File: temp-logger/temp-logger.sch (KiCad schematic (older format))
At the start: 22 parts, among them J1 USB_OTG, J2 CONN_01X03, SW1 SW_Push, SW2 SW_Push, U1 AP1117-33, U2 ESP-12E, U3 HTU21D

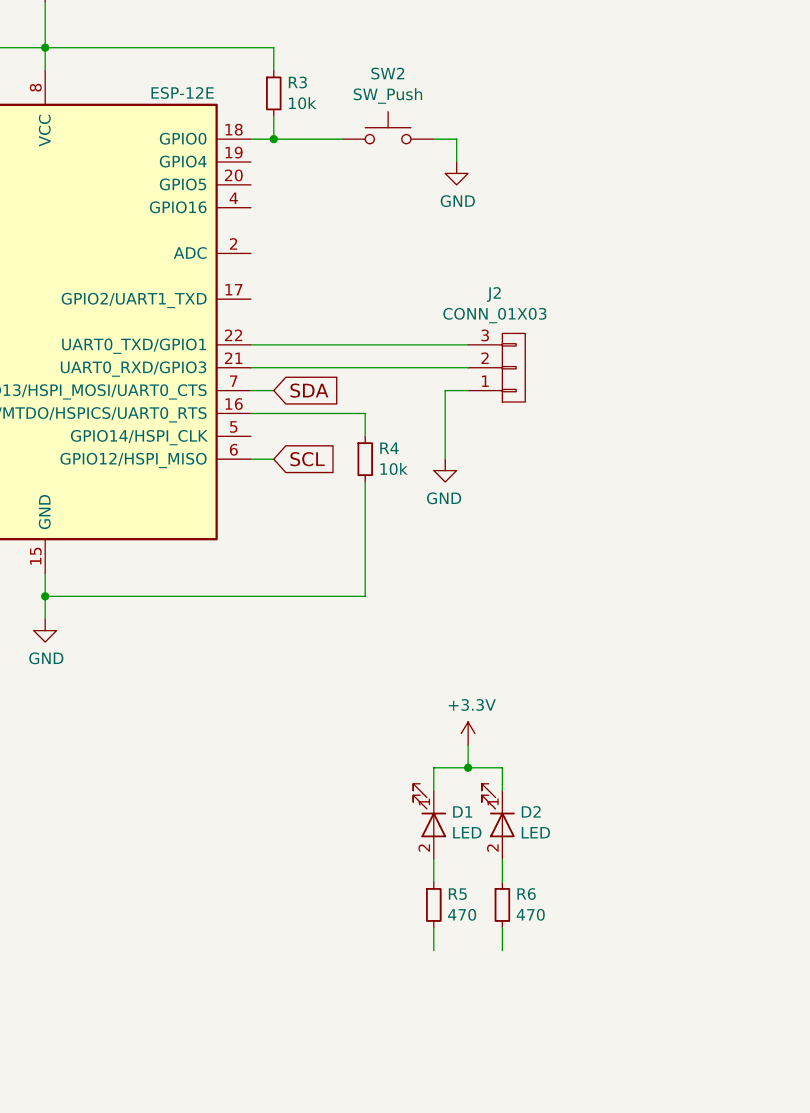
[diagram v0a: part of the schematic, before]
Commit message: Hooked up LEDs
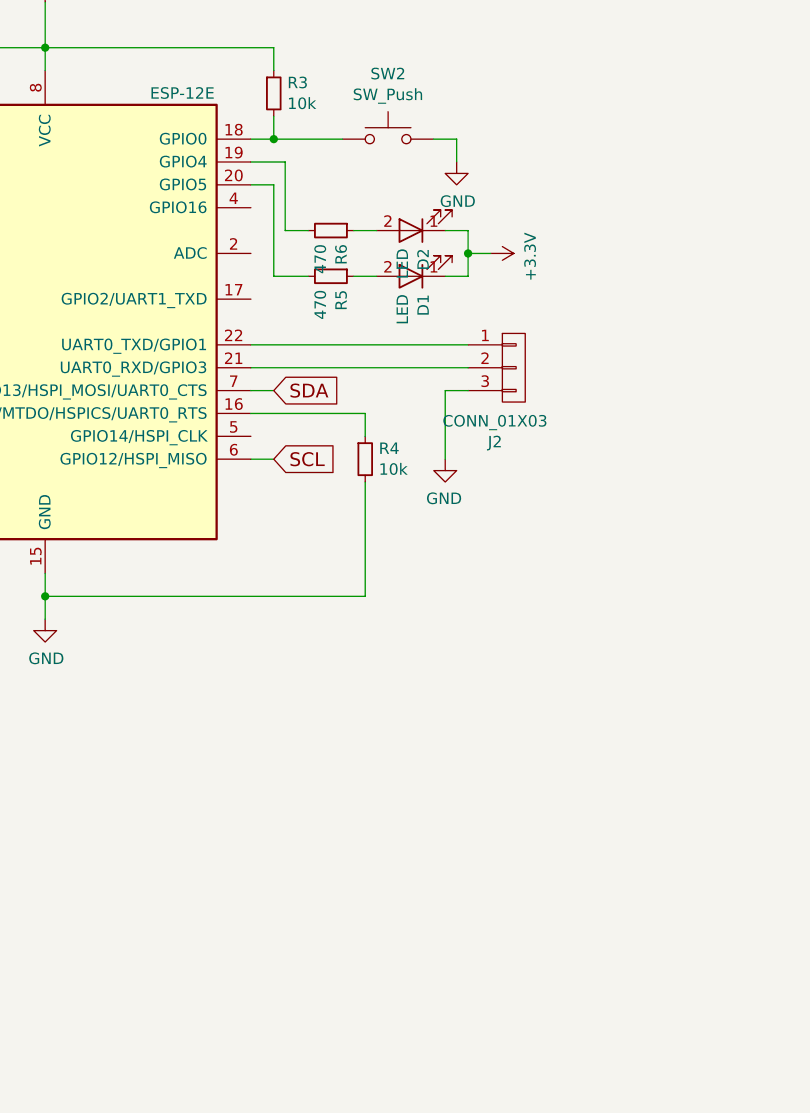
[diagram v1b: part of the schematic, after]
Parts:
- renumbered D2 to D1, D1 to D2, R6 to R5, R5 to R6
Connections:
- net GND: now also J2.3 (P3); no longer J2.1 (P1)
- net at U2.19 (GPIO4): now also R6.2
- net at U2.20 (GPIO5): now also R5.2
- net at U2.22 (UART0_TXD/GPIO1): now also J2.1 (P1); no longer J2.3 (P3)
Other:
- moved on the sheet: D1, D2, R5, R6
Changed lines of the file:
@@
+$EndComp
+$Comp
+L LED D2
+U 1 1 5A08A8EC
+P 4100 2450
+F 0 "D2" V 4045 2528 50  0000 L CNN
+F 1 "LED" V 4136 2528 50  0000 L CNN
+F 2 "LEDs:LED_0603" H 4100 2450 50  0001 C CNN
+F 3 "~" H 4100 2450 50  0001 C CNN
+	1    4100 2450
+	-1   0    0    1
 $EndComp
 $Comp
 L LED D1
-U 1 1 5A08A8EC
-P 4200 5050
-F 0 "D1" V 4145 5128 50  0000 L CNN
-F 1 "LED" V 4236 5128 50  0000 L CNN
-F 2 "LEDs:LED_0603" H 4200 5050 50  0001 C CNN
-F 3 "~" H 4200 5050 50  0001 C CNN
-	1    4200 5050
+U 1 1 5A08A96D
+P 4100 2650
+F 0 "D1" V 4045 2728 50  0000 L CNN
+F 1 "LED" V 4136 2728 50  0000 L CNN
+F 2 "LEDs:LED_0603" H 4100 2650 50  0001 C CNN
+F 3 "~" H 4100 2650 50  0001 C CNN
+	1    4100 2650
+	-1   0    0    1
+$EndComp
+$Comp
+L R_Small R6
+U 1 1 5A08AA11
+P 3750 2450
+F 0 "R6" H 3809 2496 50  0000 L CNN
+F 1 "470" H 3809 2405 50  0000 L CNN
+F 2 "Resistors_SMD:R_0603" H 3750 2450 50  0001 C CNN
+F 3 "" H 3750 2450 50  0001 C CNN
+	1    3750 2450
 	0    1    1    0
 $EndComp
 $Comp
-L LED D2
-U 1 1 5A08A96D
-P 4500 5050
-F 0 "D2" V 4445 5128 50  0000 L CNN
-F 1 "LED" V 4536 5128 50  0000 L CNN
-F 2 "LEDs:LED_0603" H 4500 5050 50  0001 C CNN
-F 3 "~" H 4500 5050 50  0001 C CNN
-	1    4500 5050
+L R_Small R5
+U 1 1 5A08AAAC
+P 3750 2650
+F 0 "R5" H 3809 2696 50  0000 L CNN
+F 1 "470" H 3809 2605 50  0000 L CNN
+F 2 "Resistors_SMD:R_0603" H 3750 2650 50  0001 C CNN
+F 3 "" H 3750 2650 50  0001 C CNN
+	1    3750 2650
 	0    1    1    0
-$EndComp
-$Comp
-L R_Small R5
-U 1 1 5A08AA11
-P 4200 5400
-F 0 "R5" H 4259 5446 50  0000 L CNN
-F 1 "470" H 4259 5355 50  0000 L CNN
-F 2 "Resistors_SMD:R_0603" H 4200 5400 50  0001 C CNN
-F 3 "" H 4200 5400 50  0001 C CNN
-	1    4200 5400
-	1    0    0    -1
-$EndComp
-$Comp
-L R_Small R6
-U 1 1 5A08AAAC
-P 4500 5400
-F 0 "R6" H 4559 5446 50  0000 L CNN
-F 1 "470" H 4559 5355 50  0000 L CNN
-F 2 "Resistors_SMD:R_0603" H 4500 5400 50  0001 C CNN
-F 3 "" H 4500 5400 50  0001 C CNN
-	1    4500 5400
-	1    0    0    -1
 $EndComp
 $Comp
 L +3.3V #PWR09
 U 1 1 5A08AB9F
-P 4350 4700
-F 0 "#PWR09" H 4350 4550 50  0001 C CNN
-F 1 "+3.3V" H 4365 4873 50  0000 C CNN
-F 2 "" H 4350 4700 50  0001 C CNN
-F 3 "" H 4350 4700 50  0001 C CNN
-	1    4350 4700
-	1    0    0    -1
+P 4450 2550
+F 0 "#PWR09" H 4450 2400 50  0001 C CNN
+F 1 "+3.3V" H 4465 2723 50  0000 C CNN
+F 2 "" H 4450 2550 50  0001 C CNN
+F 3 "" H 4450 2550 50  0001 C CNN
+	1    4450 2550
+	0    1    1    0
 $EndComp
 NoConn ~ 1600 2450
@@
 F 3 "" H 4550 3050 50  0001 C CNN
 	1    4550 3050
-	1    0    0    1
+	1    0    0    -1
 $EndComp
 Wire Wire Line
@@
 Connection ~ 2500 4050
 Wire Wire Line
-	4200 5200 4200 5300
-Wire Wire Line
-	4500 5200 4500 5300
-Wire Wire Line
-	4200 4900 4200 4800
-Wire Wire Line
-	4200 4800 4500 4800
-Wire Wire Line
-	4500 4800 4500 4900
-Wire Wire Line
-	4350 4700 4350 4800
-Connection ~ 4350 4800
-Wire Wire Line
-	4200 5500 4200 5600
-Wire Wire Line
-	4500 5500 4500 5600
+	3950 2450 3850 2450
+Wire Wire Line
+	3950 2650 3850 2650
+Wire Wire Line
+	4250 2450 4350 2450
+Wire Wire Line
+	4350 2650 4250 2650
+Wire Wire Line
+	4450 2550 4350 2550
+Connection ~ 4350 2550
+Wire Wire Line
+	3650 2450 3550 2450
+Wire Wire Line
+	3500 2650 3650 2650
 Connection ~ 1500 2050
 Wire Wire Line
@@
 Wire Wire Line
 	3500 3450 3400 3450
+Wire Wire Line
+	4350 2450 4350 2650
+Wire Wire Line
+	3400 2150 3550 2150
+Wire Wire Line
+	3550 2150 3550 2450
+Wire Wire Line
+	3400 2250 3500 2250
+Wire Wire Line
+	3500 2250 3500 2650
 $EndSCHEMATC

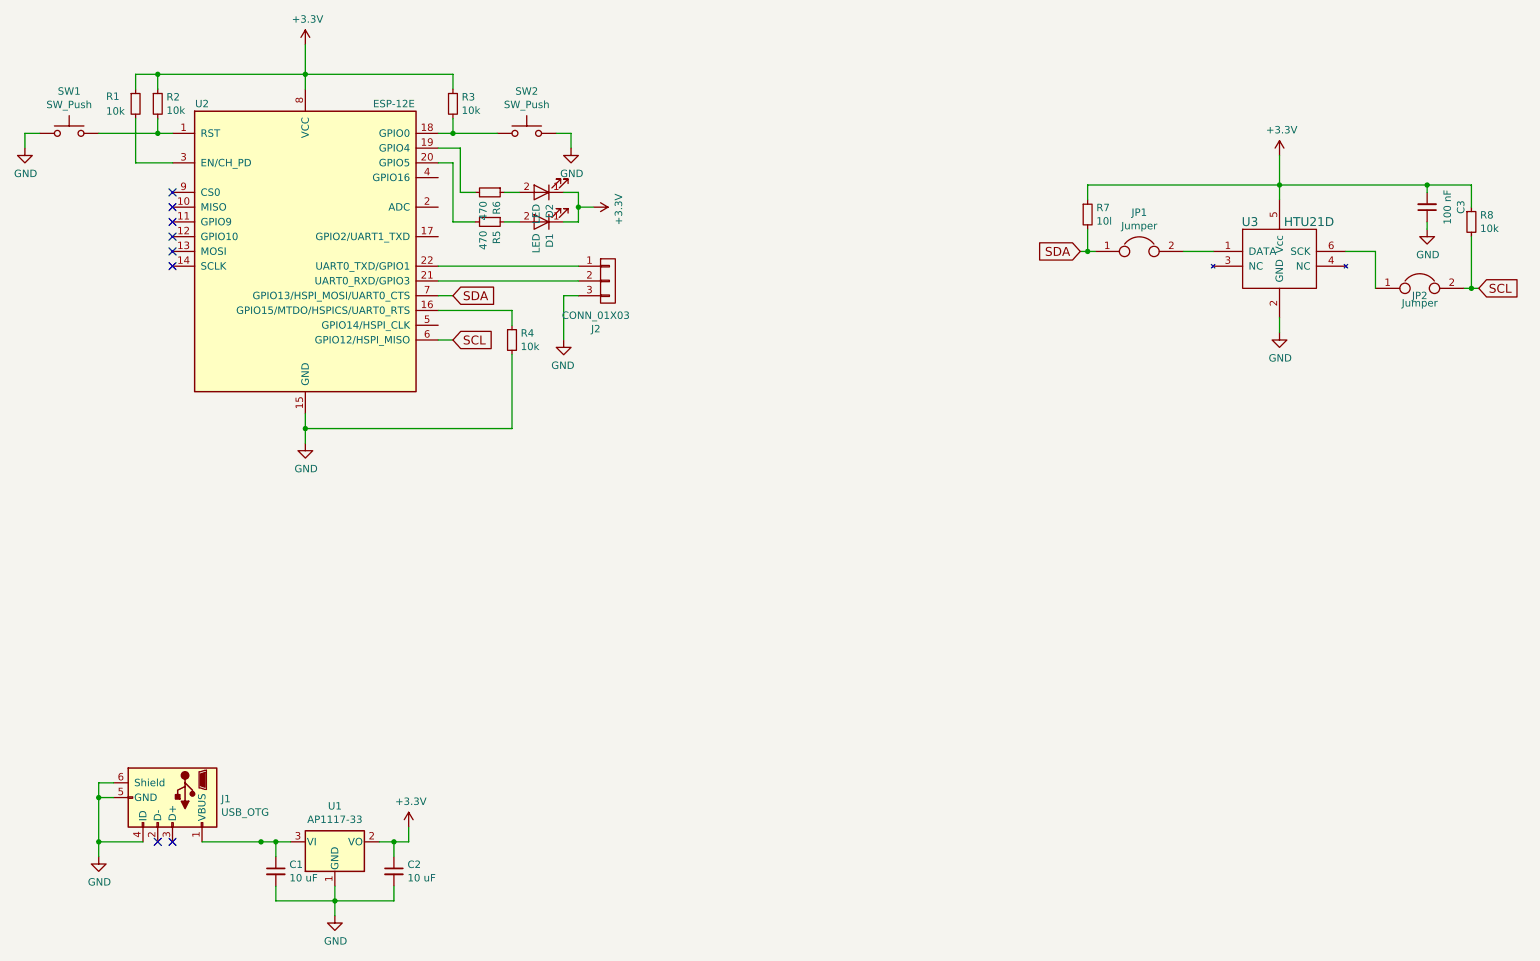
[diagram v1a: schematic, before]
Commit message: Redid layout to make soldering and programming easier
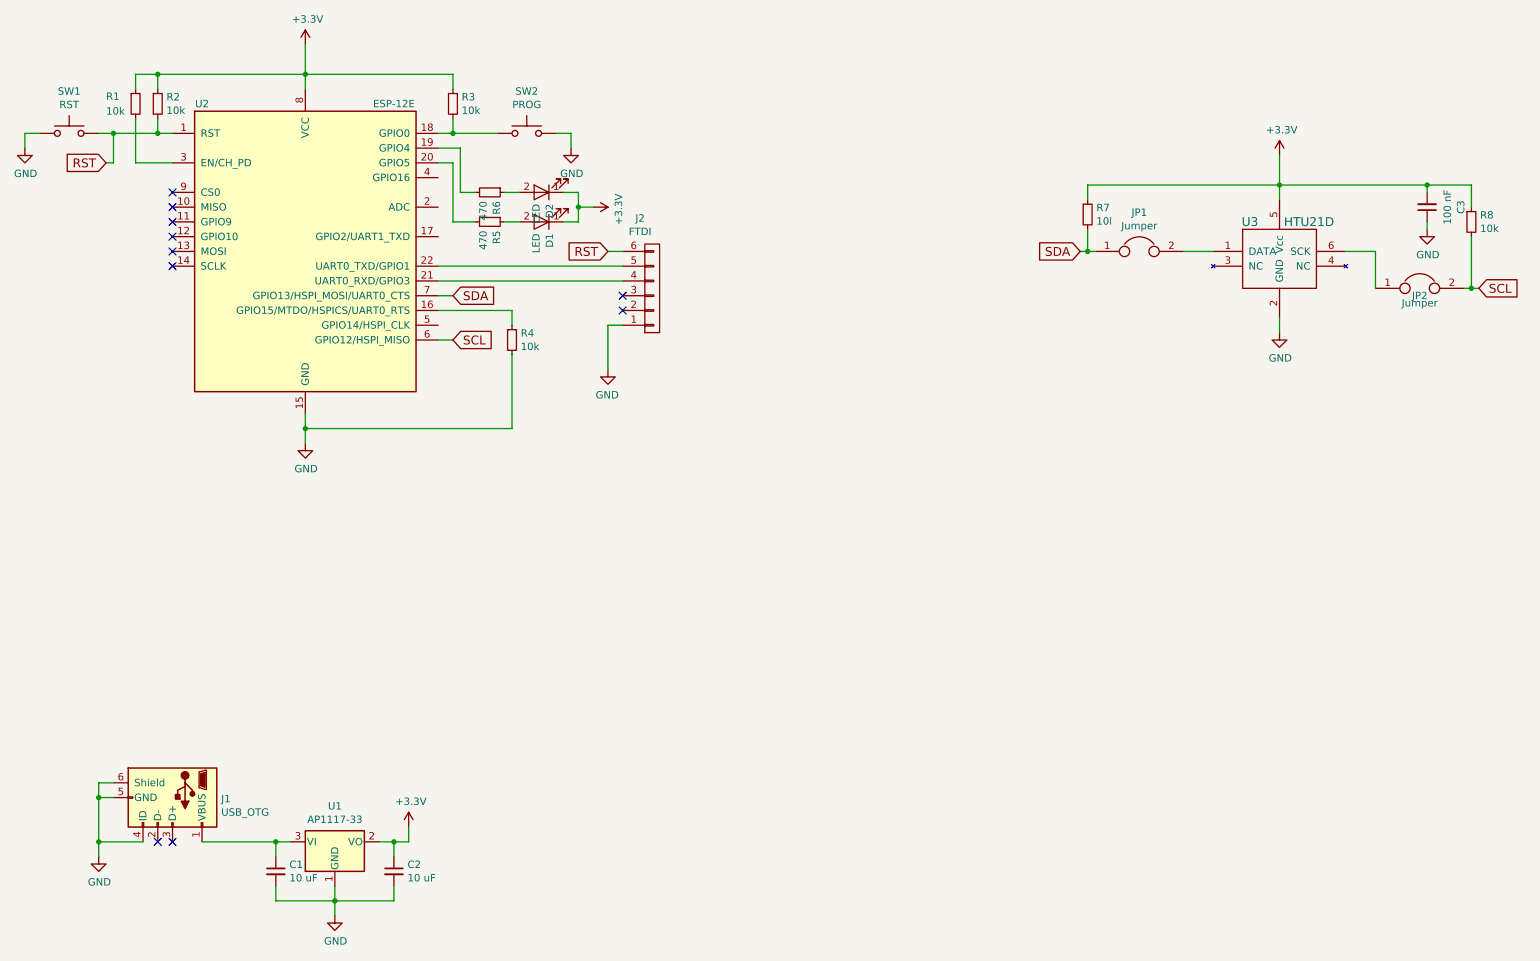
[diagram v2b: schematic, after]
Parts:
- removed J2: CONN_01X03, Pin_Headers:Pin_Header_Straight_1x03_Pitch1.00mm_SMD_Pin1Right, symbol CONN_01X03
- added J2: FTDI, Pin_Headers:Pin_Header_Straight_1x06_Pitch2.54mm, symbol CONN_01X06
- C1, C2: footprint Capacitors_SMD:C_1206 -> Capacitors_SMD:C_1206_HandSoldering
- C3: footprint Capacitors_SMD:C_0603 -> Capacitors_SMD:C_0603_HandSoldering
- D1, D2: footprint LEDs:LED_0603 -> LEDs:LED_1206_HandSoldering
- JP1, JP2, R1, R2, R3, R4, R5, R6, R7, R8: footprint Resistors_SMD:R_0603 -> Resistors_SMD:R_0603_HandSoldering
- SW1: value SW_Push -> RST
- SW2: value SW_Push -> PROG
- U1: footprint TO_SOT_Packages_SMD:SOT-223-3Lead_TabPin2 -> TO_SOT_Packages_SMD:SOT-223
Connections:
- net GND: now also J2.1 (P1)
- net RST: now reaches R2.2, SW1.2, U2.1 (RST)
- net RST: now also J2.6 (P6)
- net at U2.21 (UART0_RXD/GPIO3): now also J2.4 (P4)
- net at U2.22 (UART0_TXD/GPIO1): now also J2.5 (P5)
- no-connect marks 8 -> 10
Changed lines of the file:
@@
 F 0 "U1" H 2700 7092 50  0000 C CNN
 F 1 "AP1117-33" H 2700 7001 50  0000 C CNN
-F 2 "TO_SOT_Packages_SMD:SOT-223-3Lead_TabPin2" H 2700 7050 50  0001 C CNN
+F 2 "TO_SOT_Packages_SMD:SOT-223" H 2700 7050 50  0001 C CNN
 F 3 "http://www.diodes.com/datasheets/AP1117.pdf" H 2800 6600 50  0001 C CNN
 	1    2700 6850
@@
 F 0 "C3" V 9871 2550 50  0000 C CNN
 F 1 "100 nF" V 9962 2550 50  0000 C CNN
-F 2 "Capacitors_SMD:C_0603" H 10100 2550 50  0001 C CNN
+F 2 "Capacitors_SMD:C_0603_HandSoldering" H 10100 2550 50  0001 C CNN
 F 3 "" H 10100 2550 50  0001 C CNN
 	1    10100 2550
@@
 F 0 "C1" H 2392 7096 50  0000 L CNN
 F 1 "10 uF" H 2392 7005 50  0000 L CNN
-F 2 "Capacitors_SMD:C_1206" H 2300 7050 50  0001 C CNN
+F 2 "Capacitors_SMD:C_1206_HandSoldering" H 2300 7050 50  0001 C CNN
 F 3 "" H 2300 7050 50  0001 C CNN
 	1    2300 7050
@@
 F 0 "C2" H 3192 7096 50  0000 L CNN
 F 1 "10 uF" H 3192 7005 50  0000 L CNN
-F 2 "Capacitors_SMD:C_1206" H 3100 7050 50  0001 C CNN
+F 2 "Capacitors_SMD:C_1206_HandSoldering" H 3100 7050 50  0001 C CNN
 F 3 "" H 3100 7050 50  0001 C CNN
 	1    3100 7050
@@
 F 0 "R2" H 1559 1896 50  0000 L CNN
 F 1 "10k" H 1559 1805 50  0000 L CNN
-F 2 "Resistors_SMD:R_0603" H 1500 1850 50  0001 C CNN
+F 2 "Resistors_SMD:R_0603_HandSoldering" H 1500 1850 50  0001 C CNN
 F 3 "" H 1500 1850 50  0001 C CNN
 	1    1500 1850
@@
 F 0 "R1" H 1150 1900 50  0000 L CNN
 F 1 "10k" H 1150 1800 50  0000 L CNN
-F 2 "Resistors_SMD:R_0603" H 1350 1850 50  0001 C CNN
+F 2 "Resistors_SMD:R_0603_HandSoldering" H 1350 1850 50  0001 C CNN
 F 3 "" H 1350 1850 50  0001 C CNN
 	1    1350 1850
@@
 F 0 "R3" H 3559 1896 50  0000 L CNN
 F 1 "10k" H 3559 1805 50  0000 L CNN
-F 2 "Resistors_SMD:R_0603" H 3500 1850 50  0001 C CNN
+F 2 "Resistors_SMD:R_0603_HandSoldering" H 3500 1850 50  0001 C CNN
 F 3 "" H 3500 1850 50  0001 C CNN
 	1    3500 1850
@@
 F 0 "R4" H 3959 3496 50  0000 L CNN
 F 1 "10k" H 3959 3405 50  0000 L CNN
-F 2 "Resistors_SMD:R_0603" H 3900 3450 50  0001 C CNN
+F 2 "Resistors_SMD:R_0603_HandSoldering" H 3900 3450 50  0001 C CNN
 F 3 "" H 3900 3450 50  0001 C CNN
 	1    3900 3450
@@
 F 0 "D2" V 4045 2528 50  0000 L CNN
 F 1 "LED" V 4136 2528 50  0000 L CNN
-F 2 "LEDs:LED_0603" H 4100 2450 50  0001 C CNN
+F 2 "LEDs:LED_1206_HandSoldering" H 4100 2450 50  0001 C CNN
 F 3 "~" H 4100 2450 50  0001 C CNN
 	1    4100 2450
@@
 F 0 "D1" V 4045 2728 50  0000 L CNN
 F 1 "LED" V 4136 2728 50  0000 L CNN
-F 2 "LEDs:LED_0603" H 4100 2650 50  0001 C CNN
+F 2 "LEDs:LED_1206_HandSoldering" H 4100 2650 50  0001 C CNN
 F 3 "~" H 4100 2650 50  0001 C CNN
 	1    4100 2650
@@
 F 0 "R6" H 3809 2496 50  0000 L CNN
 F 1 "470" H 3809 2405 50  0000 L CNN
-F 2 "Resistors_SMD:R_0603" H 3750 2450 50  0001 C CNN
+F 2 "Resistors_SMD:R_0603_HandSoldering" H 3750 2450 50  0001 C CNN
 F 3 "" H 3750 2450 50  0001 C CNN
 	1    3750 2450
@@
 F 0 "R5" H 3809 2696 50  0000 L CNN
 F 1 "470" H 3809 2605 50  0000 L CNN
-F 2 "Resistors_SMD:R_0603" H 3750 2650 50  0001 C CNN
+F 2 "Resistors_SMD:R_0603_HandSoldering" H 3750 2650 50  0001 C CNN
 F 3 "" H 3750 2650 50  0001 C CNN
 	1    3750 2650
@@
 F 0 "R7" H 7859 2646 50  0000 L CNN
 F 1 "10l" H 7859 2555 50  0000 L CNN
-F 2 "Resistors_SMD:R_0603" H 7800 2600 50  0001 C CNN
+F 2 "Resistors_SMD:R_0603_HandSoldering" H 7800 2600 50  0001 C CNN
 F 3 "" H 7800 2600 50  0001 C CNN
 	1    7800 2600
@@
 F 0 "R8" H 10459 2696 50  0000 L CNN
 F 1 "10k" H 10459 2605 50  0000 L CNN
-F 2 "Resistors_SMD:R_0603" H 10400 2650 50  0001 C CNN
+F 2 "Resistors_SMD:R_0603_HandSoldering" H 10400 2650 50  0001 C CNN
 F 3 "" H 10400 2650 50  0001 C CNN
 	1    10400 2650
@@
 L GND #PWR012
 U 1 1 5A08CD0F
-P 4250 3450
-F 0 "#PWR012" H 4250 3200 50  0001 C CNN
-F 1 "GND" H 4255 3277 50  0000 C CNN
-F 2 "" H 4250 3450 50  0001 C CNN
-F 3 "" H 4250 3450 50  0001 C CNN
-	1    4250 3450
+P 4550 3650
+F 0 "#PWR012" H 4550 3400 50  0001 C CNN
+F 1 "GND" H 4555 3477 50  0000 C CNN
+F 2 "" H 4550 3650 50  0001 C CNN
+F 3 "" H 4550 3650 50  0001 C CNN
+	1    4550 3650
 	-1   0    0    -1
 $EndComp
@@
 P 900 2050
 F 0 "SW1" H 900 2335 50  0000 C CNN
-F 1 "SW_Push" H 900 2244 50  0000 C CNN
+F 1 "RST" H 900 2244 50  0000 C CNN
 F 2 "Buttons_Switches_SMD:SW_SPST_B3U-1000P" H 900 2250 50  0001 C CNN
 F 3 "" H 900 2250 50  0001 C CNN
@@
 P 4000 2050
 F 0 "SW2" H 4000 2335 50  0000 C CNN
-F 1 "SW_Push" H 4000 2244 50  0000 C CNN
+F 1 "PROG" H 4000 2244 50  0000 C CNN
 F 2 "Buttons_Switches_SMD:SW_SPST_B3U-1000P" H 4000 2250 50  0001 C CNN
 F 3 "" H 4000 2250 50  0001 C CNN
@@
 F 0 "JP1" H 8150 3114 50  0000 C CNN
 F 1 "Jumper" H 8150 3023 50  0000 C CNN
-F 2 "Resistors_SMD:R_0603" H 8150 2850 50  0001 C CNN
+F 2 "Resistors_SMD:R_0603_HandSoldering" H 8150 2850 50  0001 C CNN
 F 3 "" H 8150 2850 50  0001 C CNN
 	1    8150 2850
@@
 F 0 "JP2" H 10050 3050 50  0000 C CNN
 F 1 "Jumper" H 10050 3000 50  0000 C CNN
-F 2 "Resistors_SMD:R_0603" H 10050 3100 50  0001 C CNN
+F 2 "Resistors_SMD:R_0603_HandSoldering" H 10050 3100 50  0001 C CNN
 F 3 "" H 10050 3100 50  0001 C CNN
 	1    10050 3100
@@
 	0    1    1    0
 $EndComp
-$Comp
-L CONN_01X03 J2
-U 1 1 5A08EE6F
-P 4550 3050
-F 0 "J2" H 4468 2725 50  0000 C CNN
-F 1 "CONN_01X03" H 4468 2816 50  0000 C CNN
-F 2 "Pin_Headers:Pin_Header_Straight_1x03_Pitch1.00mm_SMD_Pin1Right" H 4550 3050 50  0001 C CNN
-F 3 "" H 4550 3050 50  0001 C CNN
-	1    4550 3050
-	1    0    0    -1
-$EndComp
 Wire Wire Line
 	2500 3950 2500 4150
@@
 	3200 6850 3200 6750
 Connection ~ 3100 6850
-Connection ~ 2200 6850
 Wire Wire Line
 	1200 6450 1100 6450
@@
 	4300 2050 4300 2150
 Wire Wire Line
-	4250 3150 4250 3450
-Wire Wire Line
-	3400 2950 4350 2950
-Wire Wire Line
-	4350 3050 3400 3050
+	4550 3350 4550 3650
+Wire Wire Line
+	3400 2950 4650 2950
+Wire Wire Line
+	3400 3050 4650 3050
 Wire Wire Line
 	7750 2850 7850 2850
@@
 Connection ~ 1100 6850
 Wire Wire Line
-	4250 3150 4350 3150
+	4550 3350 4650 3350
 Wire Wire Line
 	3900 3250 3900 3350
@@
 Wire Wire Line
 	3500 2250 3500 2650
+$Comp
+L CONN_01X06 J2
+U 1 1 5A5BC7A4
+P 4850 3100
+F 0 "J2" H 4768 2625 50  0000 C CNN
+F 1 "FTDI" H 4768 2716 50  0000 C CNN
+F 2 "Pin_Headers:Pin_Header_Straight_1x06_Pitch2.54mm" H 4850 3100 50  0001 C CNN
+F 3 "" H 4850 3100 50  0001 C CNN
+	1    4850 3100
+	1    0    0    1
+$EndComp
+NoConn ~ 4650 3250
+NoConn ~ 4650 3150
+Text GLabel 4550 2850 0    60   Input ~ 0
+RST
+Wire Wire Line
+	4550 2850 4650 2850
+Text GLabel 1150 2250 0    60   Input ~ 0
+RST
+Wire Wire Line
+	1150 2250 1200 2250
+Wire Wire Line
+	1200 2250 1200 2050
+Connection ~ 1200 2050
 $EndSCHEMATC
